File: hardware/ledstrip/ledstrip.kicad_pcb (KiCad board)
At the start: 4 copper layers, 107 x 107.5 mm, 117 parts, among them J1 Conn_ARM_JTAG_SWD_10, J2 USB_C_Receptacle_USB2.0_16P, J4 BMS connectors, J5 Ledstrip connector, J6 Header for STUSB4500 I2C, Q1 Q_NMOS, Q10 Q_PMOS, Q11 Q_NMOS, Q2 Q_NMOS, Q3 Q_NMOS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

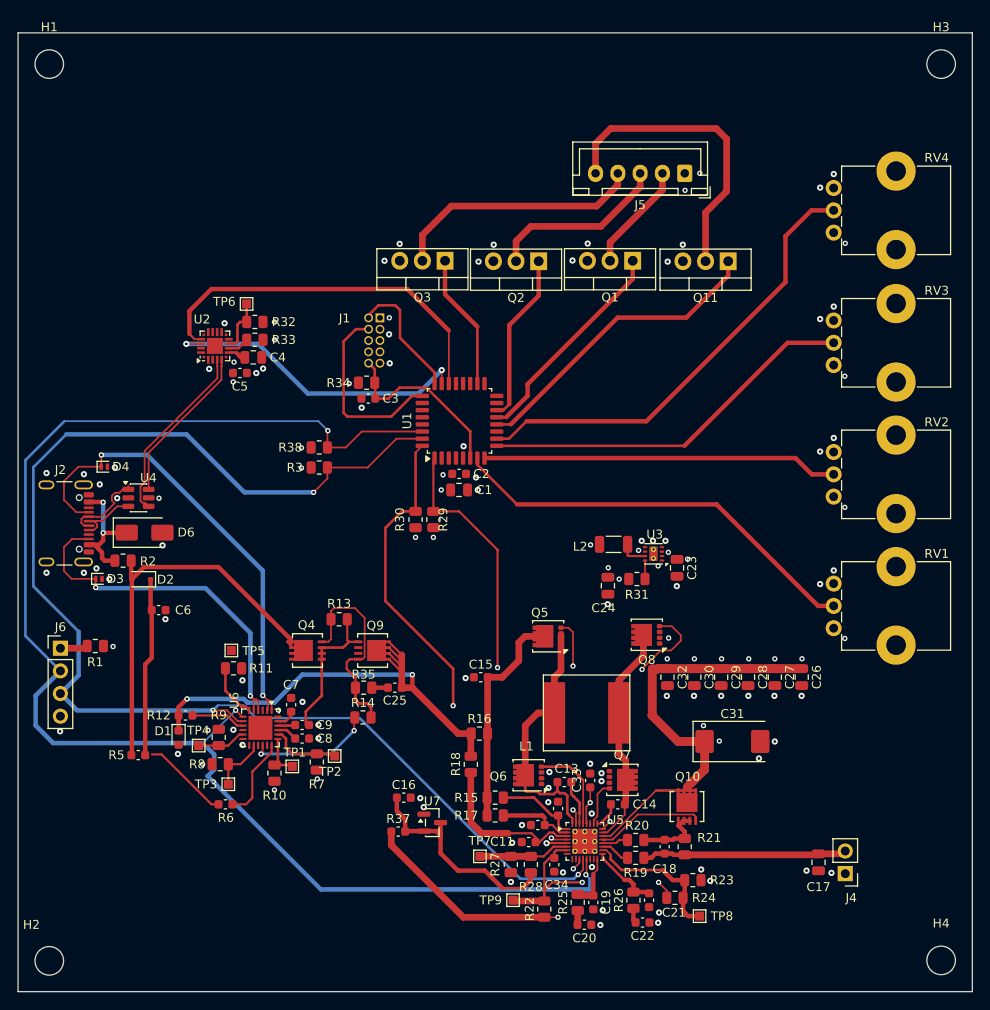
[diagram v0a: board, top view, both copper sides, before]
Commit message: Add ON/OFF button to PCB.
Decrease power zone size.
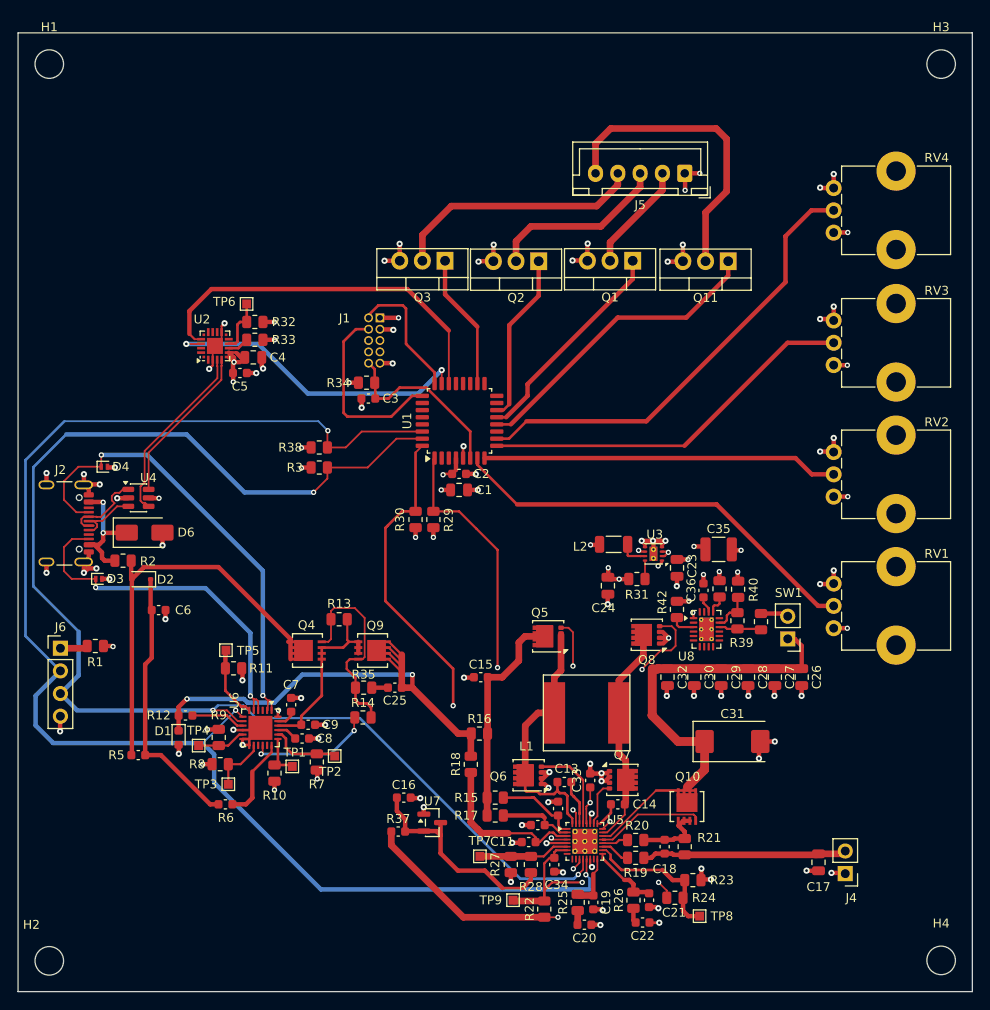
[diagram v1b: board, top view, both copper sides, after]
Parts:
- added C35: 100uF, Capacitor_SMD:C_1210_3225Metric, F.Cu at (174.8, 102.7)
- added C36: 1.5nF, Capacitor_SMD:C_0603_1608Metric, F.Cu at (173.1, 107.3)
- added R36: 17.8k, Resistor_SMD:R_0805_2012Metric, F.Cu at (174.9, 107.1)
- added R39: 16.7k, Resistor_SMD:R_0805_2012Metric, F.Cu at (176.9, 110.7)
- added R4: 475k, Resistor_SMD:R_0805_2012Metric, F.Cu at (179.6, 110.8)
- added R40: 31.2k, Resistor_SMD:R_0805_2012Metric, F.Cu at (177.0, 107.1)
- added R42: 475k, Resistor_SMD:R_0805_2012Metric, F.Cu at (170.1, 109.4)
- added SW1: SW_SPST, Connector_PinHeader_2.54mm:PinHeader_1x02_P2.54mm_Vertical, F.Cu at (182.5, 112.7)
- added U8: TPS25940, Package_DFN_QFN:QFN-20-1EP_3x4mm_P0.5mm_EP1.65x2.65mm_ThermalVias, F.Cu at (173.4, 111.6)
- moved C9 0.68 mm to (128.8, 122.3)
- moved TP5 0.61 mm to (119.6, 114.0)
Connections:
- C26 pad 1: +12V -> /Battery Charger/BQ25703A_12V_OUT
- C27 pad 1: +12V -> /Battery Charger/BQ25703A_12V_OUT
- C28 pad 1: +12V -> /Battery Charger/BQ25703A_12V_OUT
- C29 pad 1: +12V -> /Battery Charger/BQ25703A_12V_OUT
- C30 pad 1: +12V -> /Battery Charger/BQ25703A_12V_OUT
- C31 pad 1: +12V -> /Battery Charger/BQ25703A_12V_OUT
- C32 pad 1: +12V -> /Battery Charger/BQ25703A_12V_OUT
- Q10 pad D: +12V -> /Battery Charger/BQ25703A_12V_OUT
- Q8 pad S: +12V -> /Battery Charger/BQ25703A_12V_OUT
- U5 pad 22: +12V -> /Battery Charger/BQ25703A_12V_OUT
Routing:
- net GND: track 2.32 -> 131.8 mm, vias 83 -> 88
- net /Battery Charger/BQ25703A_12V_OUT: track 0.00 -> 56.1 mm
- net +3.3V: track 1.91 -> 41.2 mm
- net +12V: track 47.5 -> 9.29 mm, vias 13 -> 7
- net Net-(U8-EN_UVLO): track 0.00 -> 4.79 mm
- net Net-(U8-OVP): track 0.00 -> 4.54 mm
- net Net-(SW1-B): track 0.00 -> 3.12 mm
- net Net-(U8-PGTH): track 0.00 -> 2.79 mm
- net /USB PD/STUSB4500_VDD: track 18.5 -> 21.0 mm
- net Net-(U8-ILIM): track 0.00 -> 2.21 mm
- net /USB PD/STUSB4500_RESET: track 6.10 -> 8.15 mm
- net Net-(U8-dVdT): track 0.00 -> 1.89 mm
- net Net-(D2-A): track 44.4 -> 46.1 mm
- net Net-(D2-K): track 29.9 -> 30.6 mm
- net /Battery Charger/BQ25703A_SCL: track 164.0 -> 163.4 mm

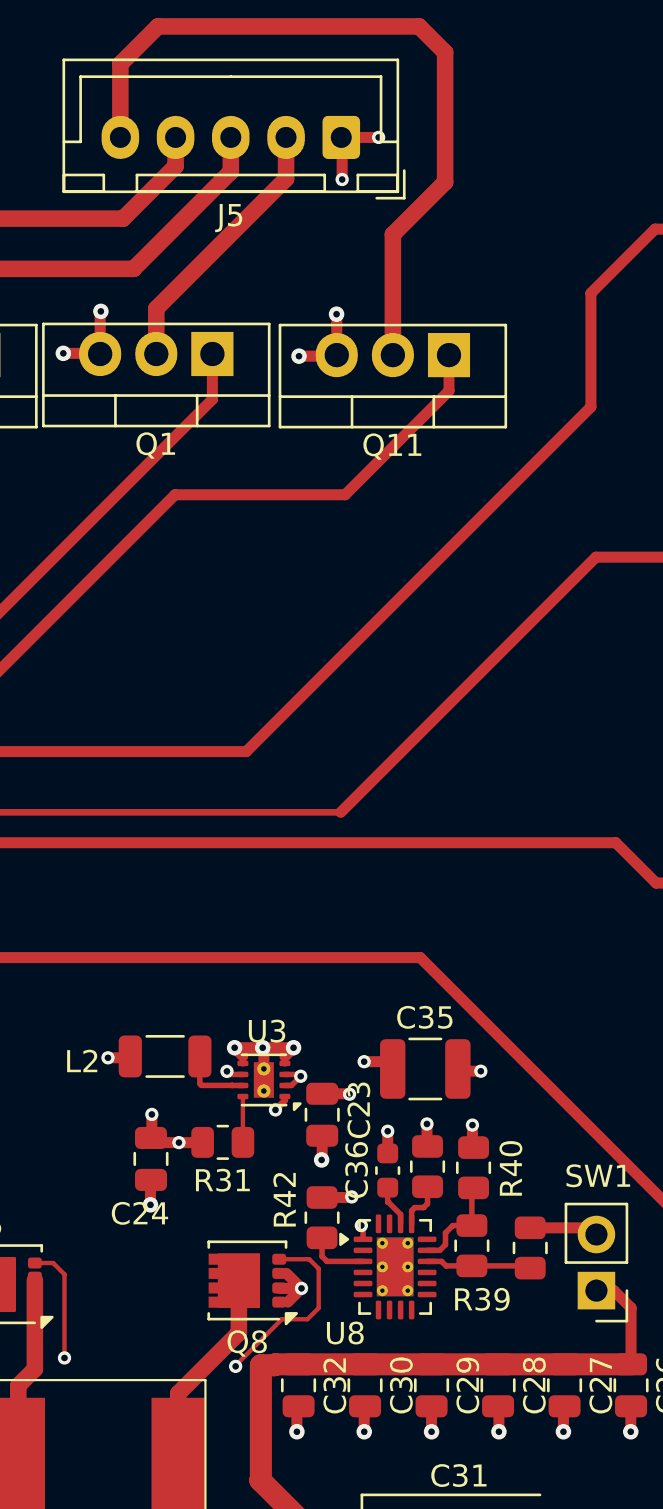
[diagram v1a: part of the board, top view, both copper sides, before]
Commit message: Remove power zones, use tracks instead.
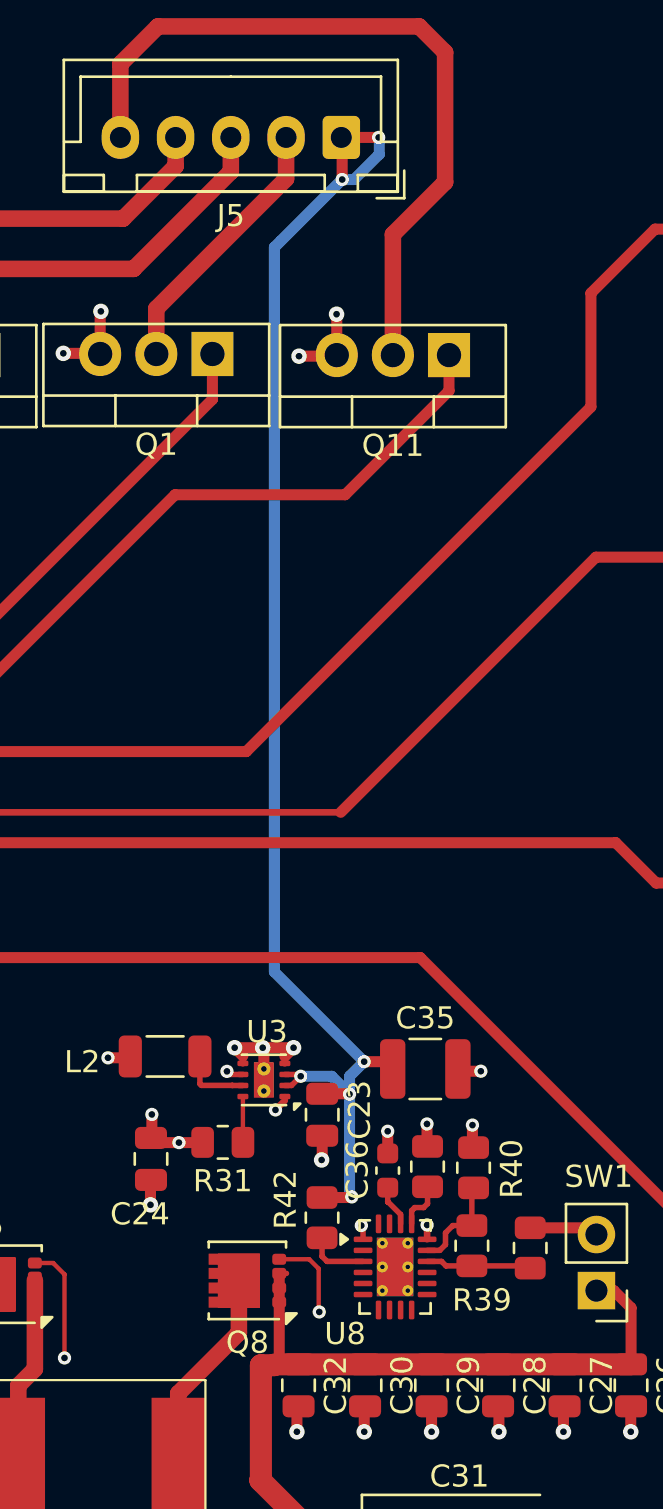
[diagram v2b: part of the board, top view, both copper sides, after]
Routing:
- net +3.3V: track 41.2 -> 323.7 mm
- net +12V: track 9.29 -> 64.1 mm, vias 7 -> 6
- net GND: track 131.8 -> 132.4 mm, vias 88 -> 89
- net /Battery Charger/BQ25703A_12V_OUT: track 56.1 -> 56.8 mm
- removed copper zone on In2.Cu, net +12V
- removed copper zone on In2.Cu, net +3.3V
